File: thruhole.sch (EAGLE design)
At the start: 12 parts

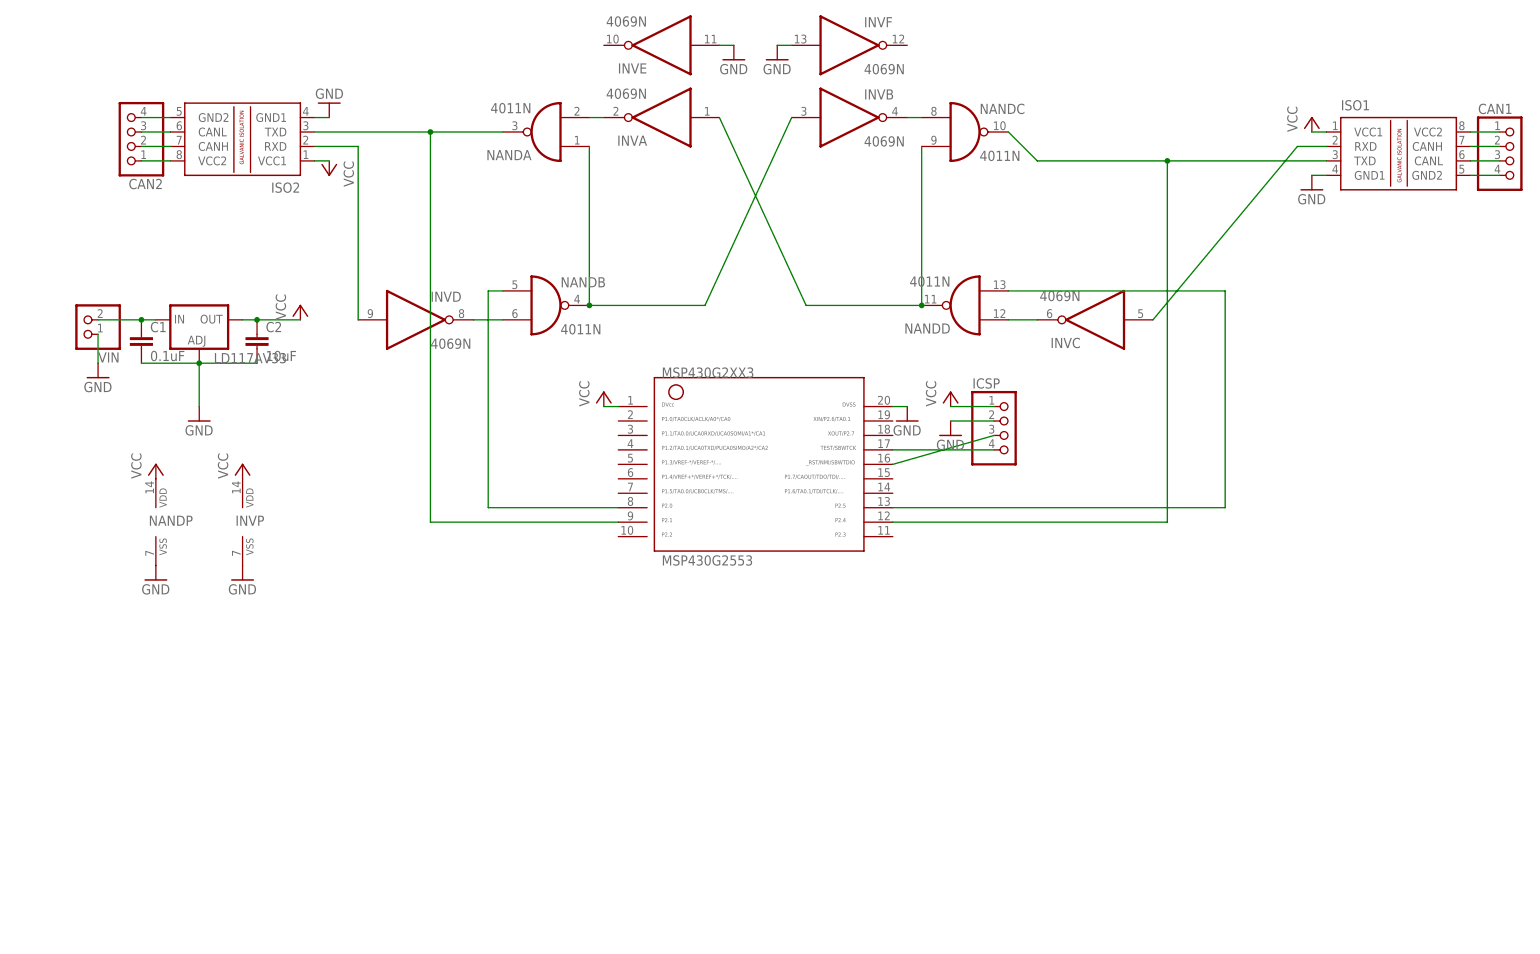
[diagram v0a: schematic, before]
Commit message: Moved components on thruhole board closer together and swapped pin headers for 1x12 pin header
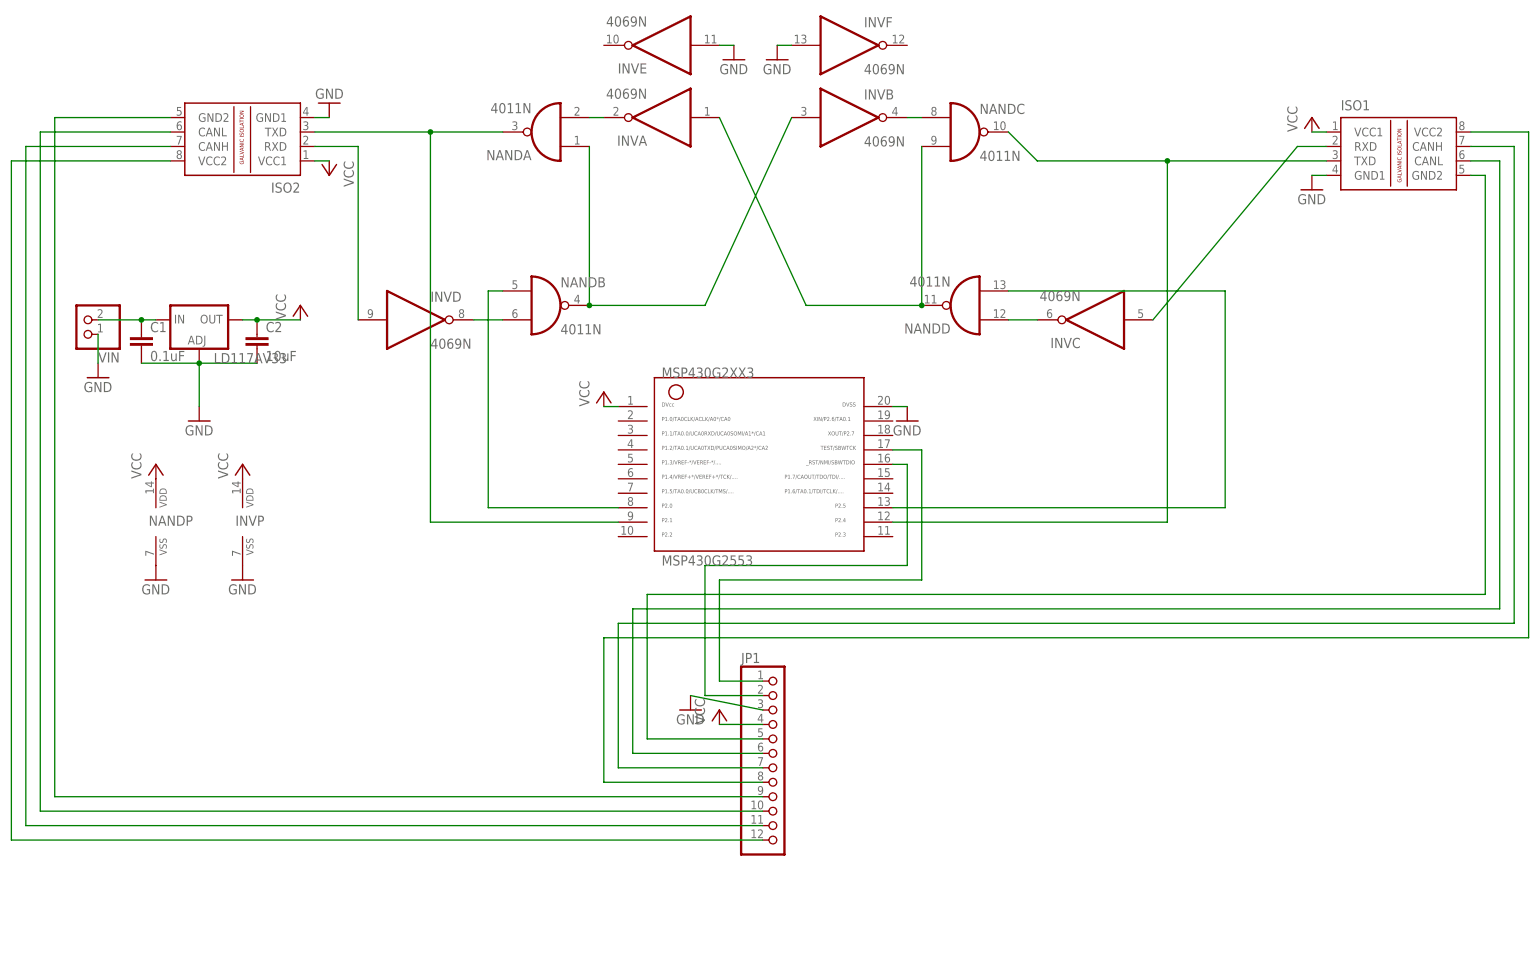
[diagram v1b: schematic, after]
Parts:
- removed CAN1, CAN2, ICSP: (no value), pinhead:PINHD-1X4
- added JP1: (no value), pinhead:PINHD-1X12
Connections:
- net GND: now also JP1.3; no longer ICSP.2
- net N$1: now also JP1.2; no longer ICSP.3
- net N$10: now also JP1.11; no longer CAN2.2
- net N$11: now also JP1.10; no longer CAN2.3
- net N$12: now also JP1.9; no longer CAN2.4
- net N$13: now also JP1.8; no longer CAN1.1
- net N$14: now also JP1.7; no longer CAN1.2
- net N$15: now also JP1.6; no longer CAN1.3
- net N$16: now also JP1.5; no longer CAN1.4
- net N$2: now also JP1.1; no longer ICSP.4
- net N$9: now also JP1.12; no longer CAN2.1
- net VCC: now also JP1.4; no longer ICSP.1
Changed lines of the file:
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@@
 <setting verticaltext="up"/>
 </settings>
-<grid distance="0.1" unitdist="inch" unit="inch" style="lines" multiple="1" display="no" altdistance="0.01" altunitdist="inch" altunit="inch"/>
+<grid distance="0.1" unitdist="inch" unit="inch" style="lines" multiple="1" display="yes" altdistance="0.01" altunitdist="inch" altunit="inch"/>
 <layers>
 <layer number="1" name="Top" color="4" fill="1" visible="no" active="no"/>
@@
 <part name="P+3" library="supply1" deviceset="VCC" device=""/>
 <part name="P+6" library="supply1" deviceset="VCC" device=""/>
-<part name="ICSP" library="pinhead" deviceset="PINHD-1X4" device=""/>
-<part name="P+7" library="supply1" deviceset="VCC" device=""/>
-<part name="GND4" library="supply1" deviceset="GND" device=""/>
 <part name="GND5" library="supply1" deviceset="GND" device=""/>
 <part name="P+4" library="supply1" deviceset="VCC" device=""/>
 <part name="GND2" library="supply1" deviceset="GND" device=""/>
-<part name="CAN2" library="pinhead" deviceset="PINHD-1X4" device=""/>
-<part name="CAN1" library="pinhead" deviceset="PINHD-1X4" device=""/>
 <part name="GND6" library="supply1" deviceset="GND" device=""/>
 <part name="GND7" library="supply1" deviceset="GND" device=""/>
@@
 <part name="GND11" library="supply1" deviceset="GND" device=""/>
 <part name="MSP430G2553" library="TI_MSP430_v16" deviceset="G2XX3---N20" device="" value=""/>
+<part name="JP1" library="pinhead" deviceset="PINHD-1X12" device=""/>
+<part name="GND9" library="supply1" deviceset="GND" device=""/>
+<part name="P+8" library="supply1" deviceset="VCC" device=""/>
 </parts>
 <sheets>
@@
 <instance part="P+3" gate="VCC" x="33.02" y="27.94"/>
 <instance part="P+6" gate="VCC" x="96.52" y="40.64"/>
-<instance part="ICSP" gate="A" x="167.64" y="33.02"/>
-<instance part="P+7" gate="VCC" x="157.48" y="40.64"/>
-<instance part="GND4" gate="1" x="157.48" y="33.02"/>
 <instance part="GND5" gate="1" x="149.86" y="35.56"/>
 <instance part="P+4" gate="VCC" x="220.98" y="88.9"/>
 <instance part="GND2" gate="1" x="220.98" y="76.2"/>
-<instance part="CAN2" gate="A" x="12.7" y="86.36" rot="R180"/>
-<instance part="CAN1" gate="A" x="256.54" y="81.28"/>
 <instance part="GND6" gate="1" x="17.78" y="7.62"/>
 <instance part="GND7" gate="1" x="33.02" y="7.62"/>
@@
 <instance part="GND11" gate="1" x="127" y="99.06"/>
 <instance part="MSP430G2553" gate="G$1" x="124.46" y="30.48"/>
+<instance part="JP1" gate="G$1" x="127" y="-22.86"/>
+<instance part="GND9" gate="1" x="111.76" y="-15.24"/>
+<instance part="P+8" gate="VCC" x="116.84" y="-15.24"/>
 </instances>
 <busses>
@@
 </segment>
 <segment>
-<pinref part="ICSP" gate="A" pin="1"/>
-<pinref part="P+7" gate="VCC" pin="VCC"/>
-<wire x1="157.48" y1="38.1" x2="165.1" y2="38.1" width="0.1524" layer="91"/>
-</segment>
-<segment>
 <pinref part="ISO1" gate="G$1" pin="VCC1"/>
 <pinref part="P+4" gate="VCC" pin="VCC"/>
@@
 <wire x1="48.26" y1="81.28" x2="45.72" y2="81.28" width="0.1524" layer="91"/>
 <pinref part="P+5" gate="VCC" pin="VCC"/>
+</segment>
+<segment>
+<pinref part="JP1" gate="G$1" pin="4"/>
+<pinref part="P+8" gate="VCC" pin="VCC"/>
+<wire x1="124.46" y1="-17.78" x2="116.84" y2="-17.78" width="0.1524" layer="91"/>
 </segment>
 </net>
@@
 </segment>
 <segment>
-<pinref part="ICSP" gate="A" pin="2"/>
-<pinref part="GND4" gate="1" pin="GND"/>
-<wire x1="157.48" y1="35.56" x2="165.1" y2="35.56" width="0.1524" layer="91"/>
-</segment>
-<segment>
 <pinref part="GND5" gate="1" pin="GND"/>
 <wire x1="149.86" y1="38.1" x2="147.32" y2="38.1" width="0.1524" layer="91"/>
@@
 <wire x1="127" y1="101.6" x2="129.54" y2="101.6" width="0.1524" layer="91"/>
 </segment>
+<segment>
+<pinref part="JP1" gate="G$1" pin="3"/>
+<pinref part="GND9" gate="1" pin="GND"/>
+<wire x1="124.46" y1="-15.24" x2="111.76" y2="-12.7" width="0.1524" layer="91"/>
+</segment>
 </net>
 <net name="N$1" class="0">
 <segment>
-<pinref part="ICSP" gate="A" pin="3"/>
-<wire x1="147.32" y1="27.94" x2="165.1" y2="33.02" width="0.1524" layer="91"/>
 <pinref part="MSP430G2553" gate="G$1" pin="16"/>
+<wire x1="147.32" y1="27.94" x2="149.86" y2="27.94" width="0.1524" layer="91"/>
+<wire x1="149.86" y1="27.94" x2="149.86" y2="10.16" width="0.1524" layer="91"/>
+<wire x1="149.86" y1="10.16" x2="114.3" y2="10.16" width="0.1524" layer="91"/>
+<wire x1="114.3" y1="10.16" x2="114.3" y2="-12.7" width="0.1524" layer="91"/>
+<pinref part="JP1" gate="G$1" pin="2"/>
+<wire x1="114.3" y1="-12.7" x2="124.46" y2="-12.7" width="0.1524" layer="91"/>
 </segment>
 </net>
 <net name="N$2" class="0">
 <segment>
-<pinref part="ICSP" gate="A" pin="4"/>
-<wire x1="147.32" y1="30.48" x2="165.1" y2="30.48" width="0.1524" layer="91"/>
+<wire x1="147.32" y1="30.48" x2="152.4" y2="30.48" width="0.1524" layer="91"/>
 <pinref part="MSP430G2553" gate="G$1" pin="17"/>
+<wire x1="152.4" y1="30.48" x2="152.4" y2="7.62" width="0.1524" layer="91"/>
+<wire x1="152.4" y1="7.62" x2="116.84" y2="7.62" width="0.1524" layer="91"/>
+<wire x1="116.84" y1="7.62" x2="116.84" y2="-10.16" width="0.1524" layer="91"/>
+<pinref part="JP1" gate="G$1" pin="1"/>
+<wire x1="116.84" y1="-10.16" x2="124.46" y2="-10.16" width="0.1524" layer="91"/>
 </segment>
 </net>
@@
 <segment>
 <pinref part="ISO1" gate="G$1" pin="VCC2"/>
-<pinref part="CAN1" gate="A" pin="1"/>
-<wire x1="254" y1="86.36" x2="248.92" y2="86.36" width="0.1524" layer="91"/>
+<wire x1="248.92" y1="86.36" x2="259.08" y2="86.36" width="0.1524" layer="91"/>
+<wire x1="259.08" y1="86.36" x2="259.08" y2="-2.54" width="0.1524" layer="91"/>
+<wire x1="259.08" y1="-2.54" x2="96.52" y2="-2.54" width="0.1524" layer="91"/>
+<pinref part="JP1" gate="G$1" pin="8"/>
+<wire x1="96.52" y1="-2.54" x2="96.52" y2="-27.94" width="0.1524" layer="91"/>
+<wire x1="96.52" y1="-27.94" x2="124.46" y2="-27.94" width="0.1524" layer="91"/>
 </segment>
 </net>
@@
 <segment>
 <pinref part="ISO1" gate="G$1" pin="CANH"/>
-<pinref part="CAN1" gate="A" pin="2"/>
-<wire x1="254" y1="83.82" x2="248.92" y2="83.82" width="0.1524" layer="91"/>
+<wire x1="256.54" y1="83.82" x2="248.92" y2="83.82" width="0.1524" layer="91"/>
+<wire x1="256.54" y1="83.82" x2="256.54" y2="0" width="0.1524" layer="91"/>
+<wire x1="256.54" y1="0" x2="99.06" y2="0" width="0.1524" layer="91"/>
+<pinref part="JP1" gate="G$1" pin="7"/>
+<wire x1="99.06" y1="0" x2="99.06" y2="-25.4" width="0.1524" layer="91"/>
+<wire x1="99.06" y1="-25.4" x2="124.46" y2="-25.4" width="0.1524" layer="91"/>
 </segment>
 </net>
@@
 <segment>
 <pinref part="ISO1" gate="G$1" pin="CANL"/>
-<pinref part="CAN1" gate="A" pin="3"/>
 <wire x1="254" y1="81.28" x2="248.92" y2="81.28" width="0.1524" layer="91"/>
+<wire x1="254" y1="81.28" x2="254" y2="2.54" width="0.1524" layer="91"/>
+<wire x1="254" y1="2.54" x2="101.6" y2="2.54" width="0.1524" layer="91"/>
+<pinref part="JP1" gate="G$1" pin="6"/>
+<wire x1="101.6" y1="2.54" x2="101.6" y2="-22.86" width="0.1524" layer="91"/>
+<wire x1="101.6" y1="-22.86" x2="124.46" y2="-22.86" width="0.1524" layer="91"/>
 </segment>
 </net>
@@
 <segment>
 <pinref part="ISO1" gate="G$1" pin="GND2"/>
-<pinref part="CAN1" gate="A" pin="4"/>
-<wire x1="254" y1="78.74" x2="248.92" y2="78.74" width="0.1524" layer="91"/>
+<wire x1="251.46" y1="78.74" x2="248.92" y2="78.74" width="0.1524" layer="91"/>
+<wire x1="251.46" y1="78.74" x2="251.46" y2="5.08" width="0.1524" layer="91"/>
+<wire x1="251.46" y1="5.08" x2="104.14" y2="5.08" width="0.1524" layer="91"/>
+<pinref part="JP1" gate="G$1" pin="5"/>
+<wire x1="104.14" y1="5.08" x2="104.14" y2="-20.32" width="0.1524" layer="91"/>
+<wire x1="104.14" y1="-20.32" x2="124.46" y2="-20.32" width="0.1524" layer="91"/>
 </segment>
 </net>
@@
 <net name="N$9" class="0">
 <segment>
-<pinref part="CAN2" gate="A" pin="1"/>
 <pinref part="ISO2" gate="G$1" pin="VCC2"/>
-<wire x1="15.24" y1="81.28" x2="20.32" y2="81.28" width="0.1524" layer="91"/>
+<wire x1="20.32" y1="81.28" x2="-7.62" y2="81.28" width="0.1524" layer="91"/>
+<wire x1="-7.62" y1="81.28" x2="-7.62" y2="-38.1" width="0.1524" layer="91"/>
+<pinref part="JP1" gate="G$1" pin="12"/>
+<wire x1="-7.62" y1="-38.1" x2="124.46" y2="-38.1" width="0.1524" layer="91"/>
 </segment>
 </net>
 <net name="N$10" class="0">
 <segment>
-<pinref part="CAN2" gate="A" pin="2"/>
 <pinref part="ISO2" gate="G$1" pin="CANH"/>
-<wire x1="15.24" y1="83.82" x2="20.32" y2="83.82" width="0.1524" layer="91"/>
+<wire x1="20.32" y1="83.82" x2="-5.08" y2="83.82" width="0.1524" layer="91"/>
+<wire x1="-5.08" y1="83.82" x2="-5.08" y2="-35.56" width="0.1524" layer="91"/>
+<pinref part="JP1" gate="G$1" pin="11"/>
+<wire x1="-5.08" y1="-35.56" x2="124.46" y2="-35.56" width="0.1524" layer="91"/>
 </segment>
 </net>
 <net name="N$11" class="0">
 <segment>
-<pinref part="CAN2" gate="A" pin="3"/>
 <pinref part="ISO2" gate="G$1" pin="CANL"/>
-<wire x1="15.24" y1="86.36" x2="20.32" y2="86.36" width="0.1524" layer="91"/>
+<wire x1="20.32" y1="86.36" x2="-2.54" y2="86.36" width="0.1524" layer="91"/>
+<wire x1="-2.54" y1="86.36" x2="-2.54" y2="-33.02" width="0.1524" layer="91"/>
+<pinref part="JP1" gate="G$1" pin="10"/>
+<wire x1="-2.54" y1="-33.02" x2="124.46" y2="-33.02" width="0.1524" layer="91"/>
 </segment>
 </net>
 <net name="N$12" class="0">
 <segment>
-<pinref part="CAN2" gate="A" pin="4"/>
 <pinref part="ISO2" gate="G$1" pin="GND2"/>
-<wire x1="15.24" y1="88.9" x2="20.32" y2="88.9" width="0.1524" layer="91"/>
-</segment>
-</net>
+<wire x1="20.32" y1="88.9" x2="0" y2="88.9" width="0.1524" layer="91"/>
+<wire x1="0" y1="88.9" x2="0" y2="-30.48" width="0.1524" layer="91"/>
+<pinref part="JP1" gate="G$1" pin="9"/>
+<wire x1="0" y1="-30.48" x2="124.46" y2="-30.48" width="0.1524" layer="91"/>
+</segment>
+</net>
